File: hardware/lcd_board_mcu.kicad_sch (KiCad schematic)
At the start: 19 parts, among them J4 Touch FPC 6P 0.5mm, J5 SWD/UART, J6 Touch alt. JST-SH 6P, SW1 BOOT (DFU), U10 STM32F072CBT6

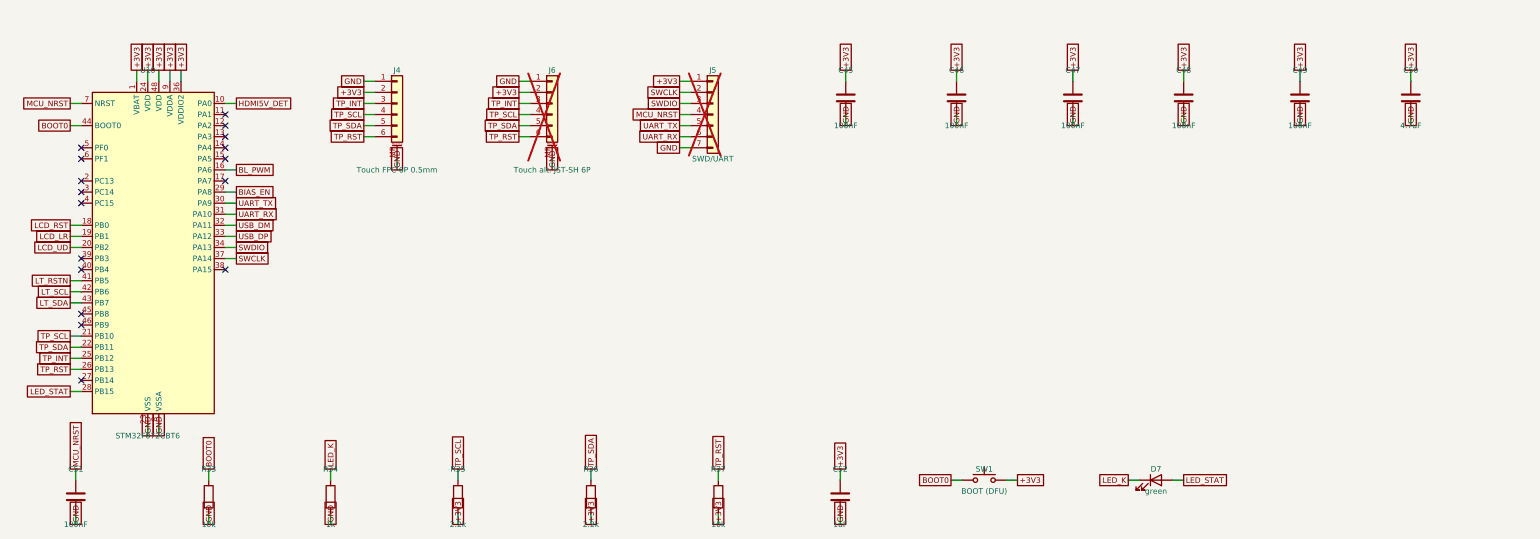
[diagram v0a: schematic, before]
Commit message: Use 0603 passives and remove the alternative touch connector J6
- All 0402 resistors/capacitors are now 0603 (LCSC numbers updated to the
  matching 0603 basic parts); bulk/high-voltage caps stay 0805/1206
- J6 (JST-SH touch header) removed
- LT8619C decoupling pre-routes, crystal and REXT placement adapted to the
  larger footprints; RGB bus escape area under the chip kept free
- Re-routed (Freerouting 2.0.1), DRC: 0 errors, 0 unconnected
- Schematic, BOM/CPL, gerbers, images and README regenerated

Co-Authored-By: Claude Opus 5.5 <noreply@anthropic.com>
Claude-Session: https://claude.ai/code/session_01X8BrieHZtCS6HfoR48ML9y
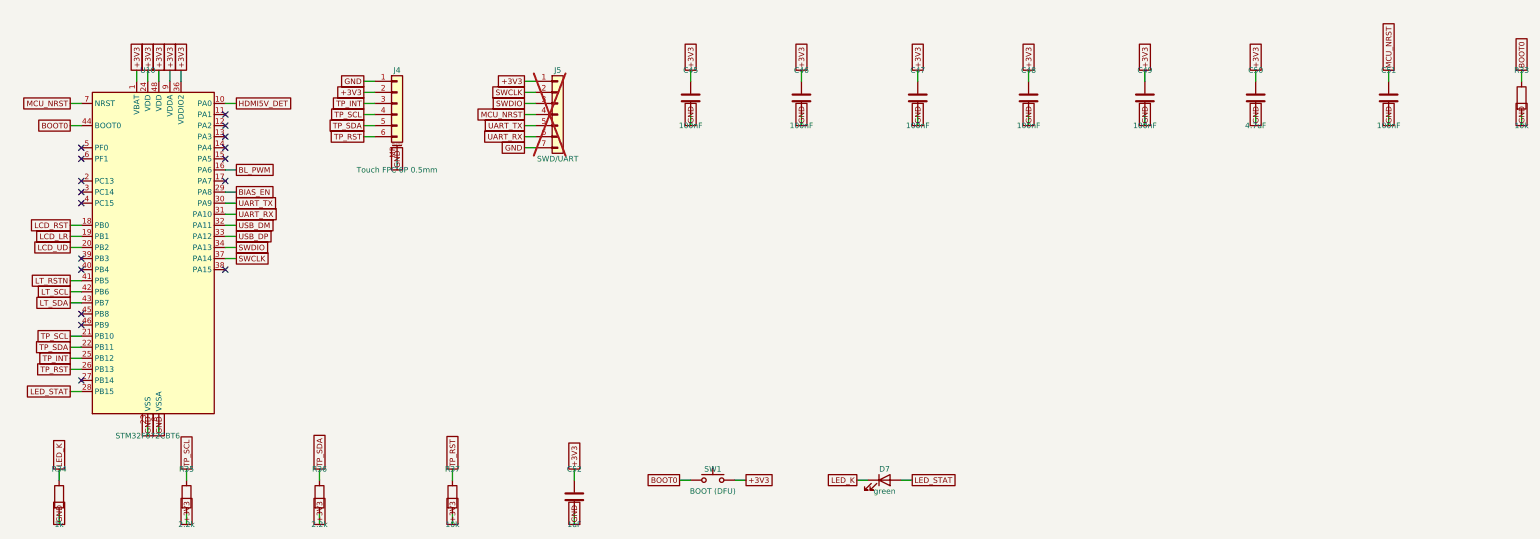
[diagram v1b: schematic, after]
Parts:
- removed J6: Touch alt. JST-SH 6P, Connector_JST:JST_SH_SM06B-SRSS-TB_1x06-1MP_P1.00mm_Horizontal, symbol Connector_Generic_MountingPin:Conn_01x06_MountingPin
- C45, C46, C47, C48, C49, C51: footprint Capacitor_SMD:C_0402_1005Metric -> Capacitor_SMD:C_0603_1608Metric; LCSC C1525 -> C14663
- C52: footprint Capacitor_SMD:C_0402_1005Metric -> Capacitor_SMD:C_0603_1608Metric; LCSC C52923 -> C15849
- R33, R37: footprint Resistor_SMD:R_0402_1005Metric -> Resistor_SMD:R_0603_1608Metric; LCSC C25744 -> C25804
- R34: footprint Resistor_SMD:R_0402_1005Metric -> Resistor_SMD:R_0603_1608Metric; LCSC C11702 -> C21190
- R35, R36: footprint Resistor_SMD:R_0402_1005Metric -> Resistor_SMD:R_0603_1608Metric
